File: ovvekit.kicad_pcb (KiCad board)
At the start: 4 copper layers, 75 x 76 mm, 123 parts, among them IC1 MAX4466EXK+T, J1 ESP_PROG_JTAG, J2 ESP_PROG_UART, J201 Power_Planes, Q201 Q_PMOS_GSD, SW1 SW_Push, SW2 SW_Push, SW3 SW_Push, U1 ESP32-WROOM-32, U201 TLV75733PDRV

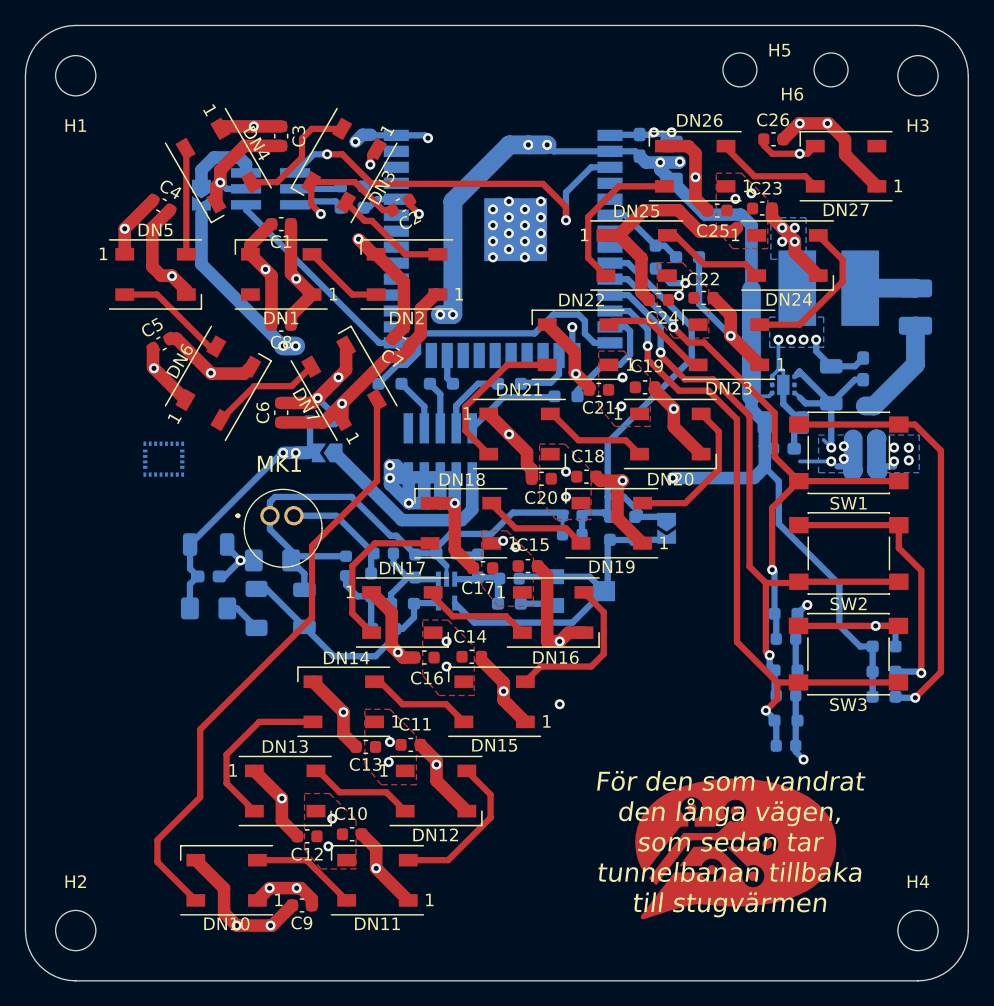
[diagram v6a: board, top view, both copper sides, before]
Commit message: Updated to kicad 6. Added AMS1117 regulator. Did more layout work in power section.
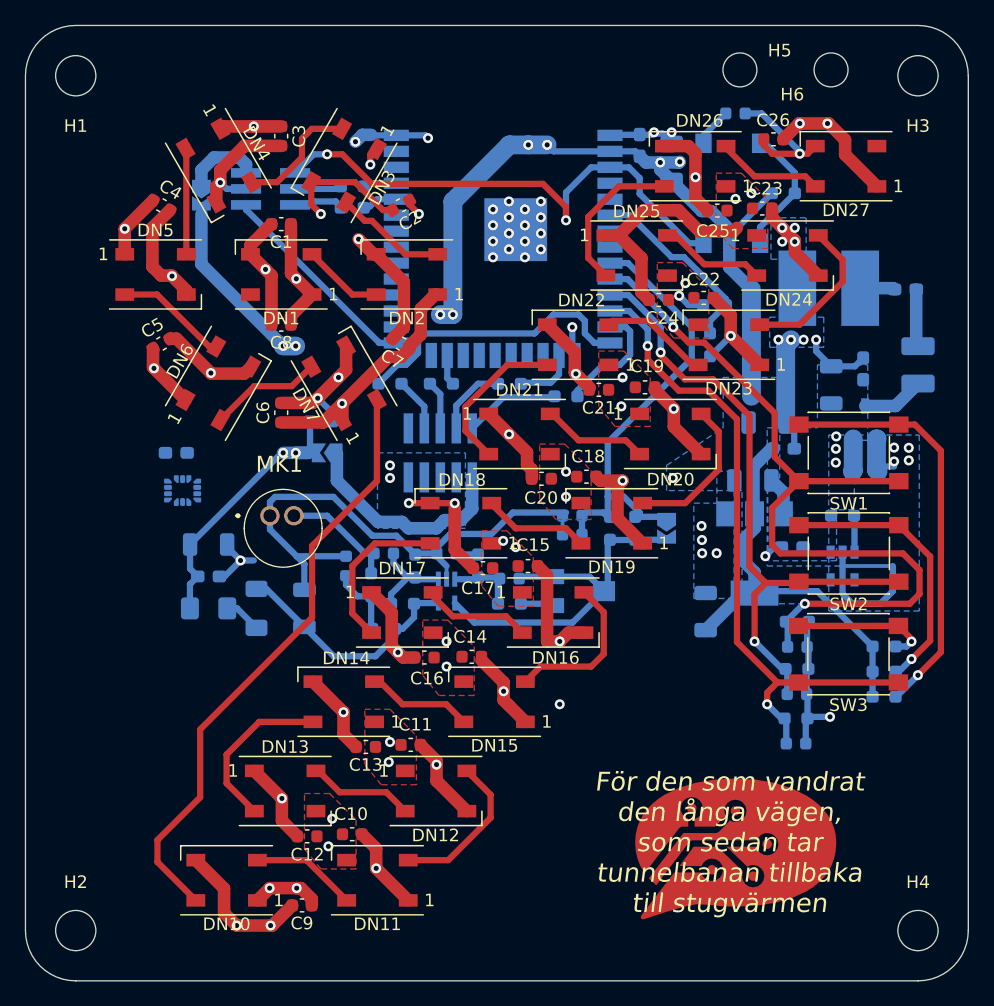
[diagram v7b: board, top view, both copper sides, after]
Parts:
- removed AC1: LSM9DS1TR, Special_Parts:LGA-24L_3X3.5X1MM_
- removed L202: L, Inductor_SMD:L_1206_3216Metric_Pad1.42x1.75mm_HandSolder
- added C110: 1uF, Capacitor_SMD:C_0603_1608Metric, B.Cu at (30.5, 0.00)
- added C211: 100n, Capacitor_SMD:C_0603_1608Metric_Pad1.08x0.95mm_HandSolder, B.Cu at (35.0, 34.5)
- added C212: 10uF, Capacitor_SMD:C_1206_3216Metric, B.Cu at (31.9, 29.2)
- added C213: 10uF, Capacitor_SMD:C_1206_3216Metric, B.Cu at (28.1, 39.6)
- added C31: 100n, Capacitor_SMD:C_0603_1608Metric_Pad1.08x0.95mm_HandSolder, B.Cu at (-14.0, 27.0)
- added FB1: FerriteBead_Small, Capacitor_SMD:C_0603_1608Metric_Pad1.08x0.95mm_HandSolder, B.Cu at (44.0, 14.0)
- added R111: 220R, Resistor_SMD:R_0603_1608Metric_Pad0.98x0.95mm_HandSolder, B.Cu at (34.3, 6.35)
- added R220: 100K, Resistor_SMD:R_0603_1608Metric_Pad0.98x0.95mm_HandSolder, B.Cu at (39.0, 32.0)
- added SW4: SW_Push, Button_Switch_SMD:SW_Push_1P1T_NO_6x6mm_H9.5mm, B.Cu at (30.2, 6.35)
- added U202: LSM6DS3, Package_LGA:LGA-14_3x2.5mm_P0.5mm_LayoutBorder3x4y, B.Cu at (-13.5, 30.0)
- added U203: AMS1117-3.3, Package_TO_SOT_SMD:SOT-223-3_TabPin2, B.Cu at (32.0, 35.0)
- U201: value TLV75733PDRV -> AP2112K-3.3; footprint Package_SON:WSON-6-1EP_2x2mm_P0.65mm_EP1x1.6mm -> Package_TO_SOT_SMD:SOT-23-5
- moved U201 15.2 mm to (39.0, 36.0), turned to -90 degrees
- moved R201 7.19 mm to (28.5, 18.4), turned to 90 degrees
- moved R202 6.03 mm to (28.8, 15.2), turned to 180 degrees
- moved F201 4.60 mm to (45.0, 20.0)
- moved svg2mod 1.80 mm to (-17.0, 51.0)
- moved C202 1.29 mm to (33.0, 24.6)
- moved C100 1.10 mm to (35.4, 42.4)
- moved R102 1.10 mm to (35.4, 40.4)
- moved C101 0.88 mm to (35.4, 46.2)
- moved R104 0.88 mm to (35.4, 44.2)
- moved C102 0.82 mm to (35.3, 50.1)
- moved R106 0.82 mm to (35.3, 48.1)
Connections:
- DN1 pad 4: Net-(DN1-Pad4) -> unconnected-(DN1-Pad4)
- DN27 pad 2: Net-(DN27-Pad2) -> unconnected-(DN27-Pad2)
- J1 pad 10: Net-(J1-Pad10) -> unconnected-(J1-Pad10)
- J201 pad 1: Net-(F201-Pad1) -> Net-(FB1-Pad1)
- U1 pad 17: Net-(U1-Pad17) -> unconnected-(U1-Pad17)
- U1 pad 18: Net-(U1-Pad18) -> unconnected-(U1-Pad18)
- U1 pad 19: Net-(U1-Pad19) -> unconnected-(U1-Pad19)
- U1 pad 20: Net-(U1-Pad20) -> unconnected-(U1-Pad20)
- U1 pad 21: Net-(U1-Pad21) -> unconnected-(U1-Pad21)
- U1 pad 22: Net-(U1-Pad22) -> unconnected-(U1-Pad22)
- U1 pad 24: Net-(U1-Pad24) -> unconnected-(U1-Pad24)
- U1 pad 26: Net-(U1-Pad26) -> unconnected-(U1-Pad26)
- U1 pad 27: Net-(U1-Pad27) -> unconnected-(U1-Pad27)
- U1 pad 28: Net-(U1-Pad28) -> unconnected-(U1-Pad28)
- U1 pad 29: Net-(U1-Pad29) -> unconnected-(U1-Pad29)
- U1 pad 3: EN -> RESET
- U1 pad 30: Net-(U1-Pad30) -> unconnected-(U1-Pad30)
- U1 pad 31: Net-(U1-Pad31) -> unconnected-(U1-Pad31)
- U1 pad 32: Net-(U1-Pad32) -> unconnected-(U1-Pad32)
- U1 pad 33: Net-(U1-Pad33) -> unconnected-(U1-Pad33)
- U1 pad 36: Net-(U1-Pad36) -> unconnected-(U1-Pad36)
- U1 pad 37: Net-(U1-Pad37) -> unconnected-(U1-Pad37)
- U1 pad 4: Net-(U1-Pad4) -> unconnected-(U1-Pad4)
- U1 pad 5: Net-(U1-Pad5) -> unconnected-(U1-Pad5)
- U1 pad 7: Net-(U1-Pad7) -> unconnected-(U1-Pad7)
- U1 pad 8: Net-(U1-Pad8) -> unconnected-(U1-Pad8)
- U201 pad 1: +3V3 -> VCC
- U201 pad 2: Net-(U201-Pad2) -> GND
- U201 pad 3: GND -> Net-(R220-Pad2)
- U201 pad 4: VCC -> unconnected-(U201-Pad4)
- U201 pad 5: Net-(U201-Pad5) -> +3V3
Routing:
- net RESET: track 0.00 -> 45.3 mm, vias 0 -> 2
- net EN: track 31.5 -> 0.00 mm, vias 2 -> 0
- net BTN_1: track 45.4 -> 65.8 mm
- net VCC: track 160.5 -> 140.1 mm, vias 30 -> 29
- net GND: track 233.8 -> 223.1 mm, vias 65 -> 69
- net Net-(R111-Pad2): track 0.00 -> 10.5 mm
- net Battery_monitor: track 6.64 -> 15.2 mm
- net Net-(F201-Pad2): track 8.45 -> 4.94 mm
- net Net-(R220-Pad2): track 0.00 -> 2.92 mm
- net Net-(FB1-Pad1): track 0.00 -> 2.78 mm
- net +3V3: track 151.2 -> 149.5 mm
- net Net-(J1-Pad1): track 16.0 -> 17.7 mm
- net BTN_2: track 50.1 -> 51.3 mm
- net Net-(R101-Pad2): track 34.3 -> 33.3 mm
- net Net-(R103-Pad2): track 22.6 -> 22.0 mm
- added copper zone on B.Cu, net +3V3
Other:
- net class Default removed
- net class audio removed

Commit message: Updated PCB after DRC. Updated Connector lib.
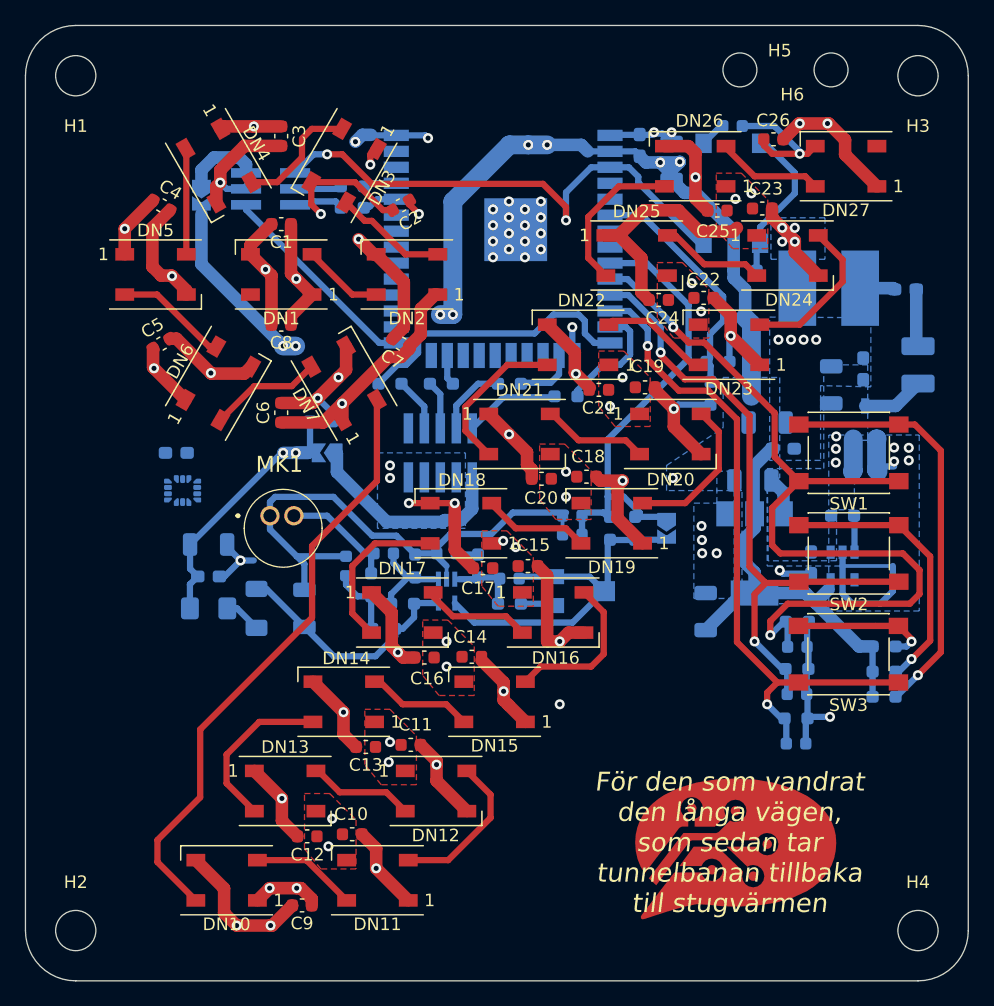
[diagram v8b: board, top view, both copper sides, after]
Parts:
- moved R202 7.02 mm to (28.5, 22.2), turned to -90 degrees
- moved R111 6.86 mm to (31.2, 12.5)
- moved C211 1.95 mm to (36.5, 35.8), turned to -90 degrees
- moved R201 1.49 mm to (29.1, 19.8), turned to 180 degrees
- moved C110 1.03 mm to (30.2, 1.00)
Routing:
- net GND: track 223.1 -> 210.2 mm
- net BTN_1: track 65.8 -> 69.8 mm
- net Battery_monitor: track 15.2 -> 19.1 mm
- net Net-(R111-Pad2): track 10.5 -> 12.8 mm
- net RESET: track 45.3 -> 43.8 mm
- net Net-(J1-Pad1): track 17.7 -> 16.9 mm
- net AUDIO_OUT: track 35.9 -> 36.6 mm
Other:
- board text added: "JLCJLCJLCJLC"
